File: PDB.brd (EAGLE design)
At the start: 160 x 100 mm, 60 parts, among them IC1 LM555N

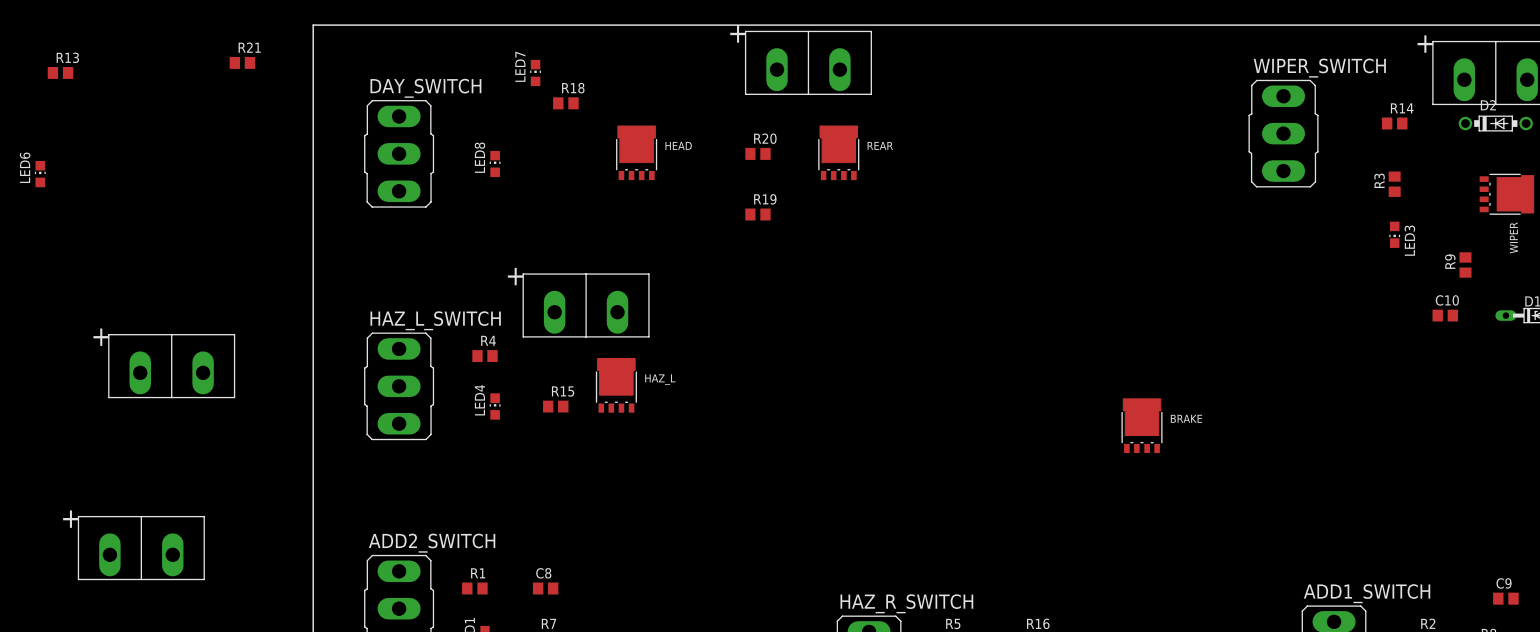
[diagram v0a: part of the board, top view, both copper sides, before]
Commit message: ratsnest to remove some airwires
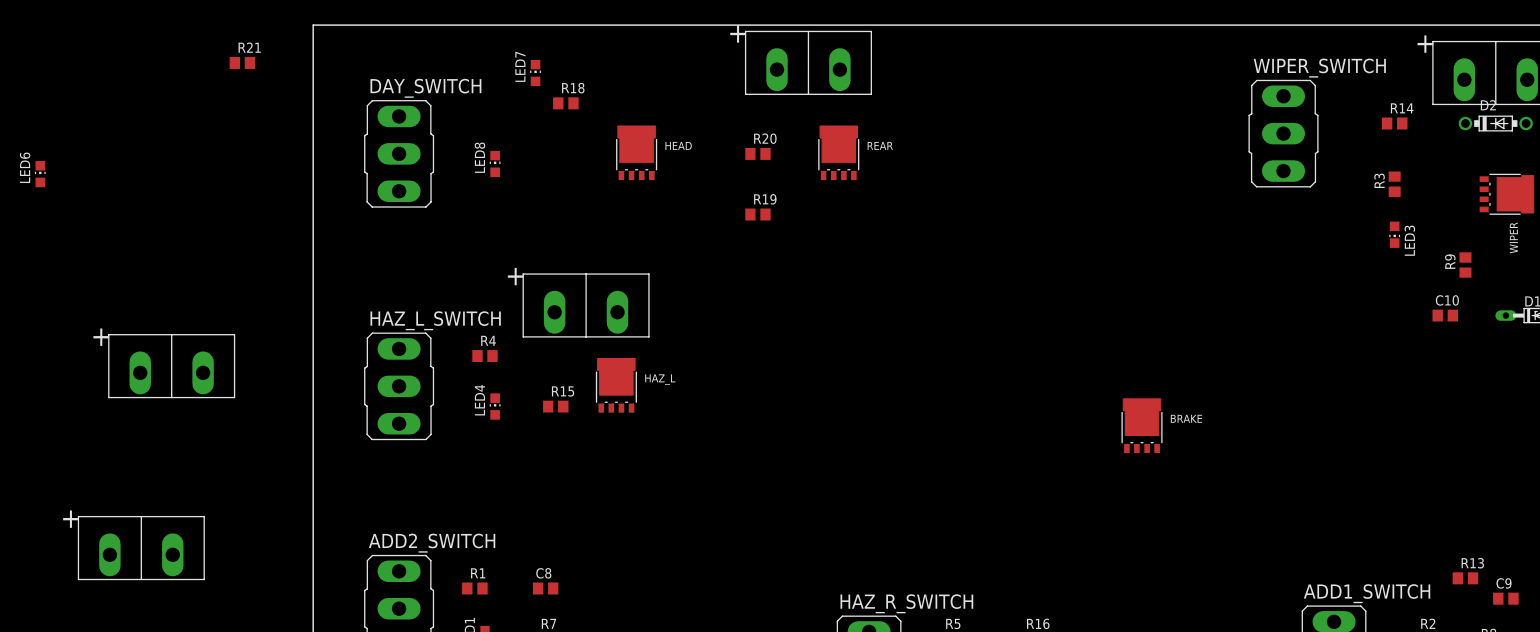
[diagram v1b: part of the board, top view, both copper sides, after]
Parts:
- moved R13 187.6 mm to (144.8, 30.5)

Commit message: updated board layout
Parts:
- removed ADD2_OUT1, ADD2_OUT2, ADD2_OUT3, ADD2_OUT4, ADD2_OUT5, ADD2_OUT6, ADD2_OUT7: POWERPOLE_POWER25A, powerpoles:POWERPOLE_PAIR_25A
- removed BRAKE_SENSOR, DAY_SWITCH: (no value), switch:M9040P
- added ADD1_OUT, BRAKE_OUT, HAZL_OUT, HAZR_OUT, HEADLIGHTS_OUT, REARLIGHTS_OUT, VDD_IN1, WIPER_OUT: POWERPOLE_POWER25A_HORIZONTAL_G2, powerpoles:POWERPOLE_PAIR_25A_HORIZ_G2
- added BRAKE_SNS_OVR, HEADLIGHTS, REARLIGHTS: (no value), switch:M9040P
- ADD2_OUT, VDD_IN: value POWERPOLE_POWER25A -> POWERPOLE_POWER25A_HORIZONTAL_G2; device powerpoles:POWERPOLE_PAIR_25A -> powerpoles:POWERPOLE_PAIR_25A_HORIZ_G2
- moved R21 129.9 mm to (120.7, 85.1)
- moved D2 94.8 mm to (97.8, 7.62)
- moved HAZ_R 94.0 mm to (148.6, 88.9), turned to 180 degrees
- moved LED7 92.7 mm to (120.7, 91.4)
- moved LED5 91.6 mm to (143.5, 82.5), turned to 180 degrees
- moved R5 90.9 mm to (139.7, 91.4), turned to 180 degrees
- moved HAZ_R_SWITCH 82.8 mm to (139.7, 63.5), turned to 180 degrees
- moved R16 79.8 mm to (138.4, 86.4), turned to 180 degrees
- moved BRAKE 78.6 mm to (36.8, 90.2), turned to 270 degrees
- moved R17 78.5 mm to (33.0, 81.3), turned to 270 degrees
- moved D1 77.8 mm to (92.7, 15.2), turned to 180 degrees
- moved VDD_IN 73.7 mm to (-11.4, -3.81), turned to 180 degrees
- moved WIPER 73.4 mm to (105.4, 20.3)
- moved R6 72.6 mm to (25.4, 83.8), turned to 180 degrees
- moved LED8 71.2 mm to (94.0, 85.1)
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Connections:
- new net H8: HEADLIGHTS.1, R18.1
- net GND: now also VDD_IN1.BLACK
- net H1: now also BRAKE_SNS_OVR.1, VDD_IN1.RED; no longer BRAKE_SENSOR.1
- net H7: now also REARLIGHTS.1; no longer DAY_SWITCH.1, R18.1
- net N$1: now also HEADLIGHTS_OUT.BLACK; no longer ADD2_OUT6.BLACK
- net N$17: now also ADD1_OUT.BLACK; no longer ADD2_OUT1.BLACK
- net N$18: now also ADD1_OUT.RED; no longer ADD2_OUT1.RED
- net N$19: now also WIPER_OUT.BLACK; no longer ADD2_OUT2.BLACK
- net N$20: now also WIPER_OUT.RED; no longer ADD2_OUT2.RED
- net N$21: now also HAZL_OUT.BLACK; no longer ADD2_OUT3.BLACK
- net N$23: now also HAZR_OUT.BLACK; no longer ADD2_OUT4.BLACK
- net N$25: now also BRAKE_OUT.BLACK; no longer ADD2_OUT5.BLACK
- net N$3: now also REARLIGHTS_OUT.BLACK; no longer ADD2_OUT7.BLACK
- net VDD: now also BRAKE_OUT.RED, BRAKE_SNS_OVR.2, HAZL_OUT.RED, HAZR_OUT.RED, HEADLIGHTS.2, HEADLIGHTS_OUT.RED, REARLIGHTS.2, REARLIGHTS_OUT.RED; no longer ADD2_OUT3.RED, ADD2_OUT4.RED, ADD2_OUT5.RED, ADD2_OUT6.RED, ADD2_OUT7.RED, BRAKE_SENSOR.2, DAY_SWITCH.2
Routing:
- added copper zone on layer 16, net GND
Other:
- board size 160 x 100 mm -> 209.5 x 127.9 mm

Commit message: board layout
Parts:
- moved ADD2 58.5 mm to (96.5, 25.4), turned to 270 degrees
- moved R1 49.7 mm to (87.6, 15.2)
- moved LED1 48.1 mm to (86.4, 22.9), turned to 180 degrees
- moved ADD2_OUT 40.8 mm to (83.8, -1.27)
- moved ADD2_SWITCH 39.4 mm to (88.3, 41.9)
- moved VDD_IN 38.1 mm to (26.7, -2.54)
- moved C8 32.0 mm to (78.7, 22.9)
- moved R7 32.0 mm to (78.7, 16.5)
- moved R12 30.6 mm to (81.3, 29.2)
- moved D1 22.9 mm to (111.8, 27.9)
- moved WIPER_OUT 19.7 mm to (116.8, -1.27)
- moved C10 19.4 mm to (114.3, 22.9)
- moved D2 19.4 mm to (116.8, 11.4)
- moved ADD1 19.1 mm to (149.9, 27.9), turned to 270 degrees
- moved R3 19.1 mm to (128.3, 27.9)
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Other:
- board size 209.5 x 127.9 mm -> 198.1 x 127.9 mm

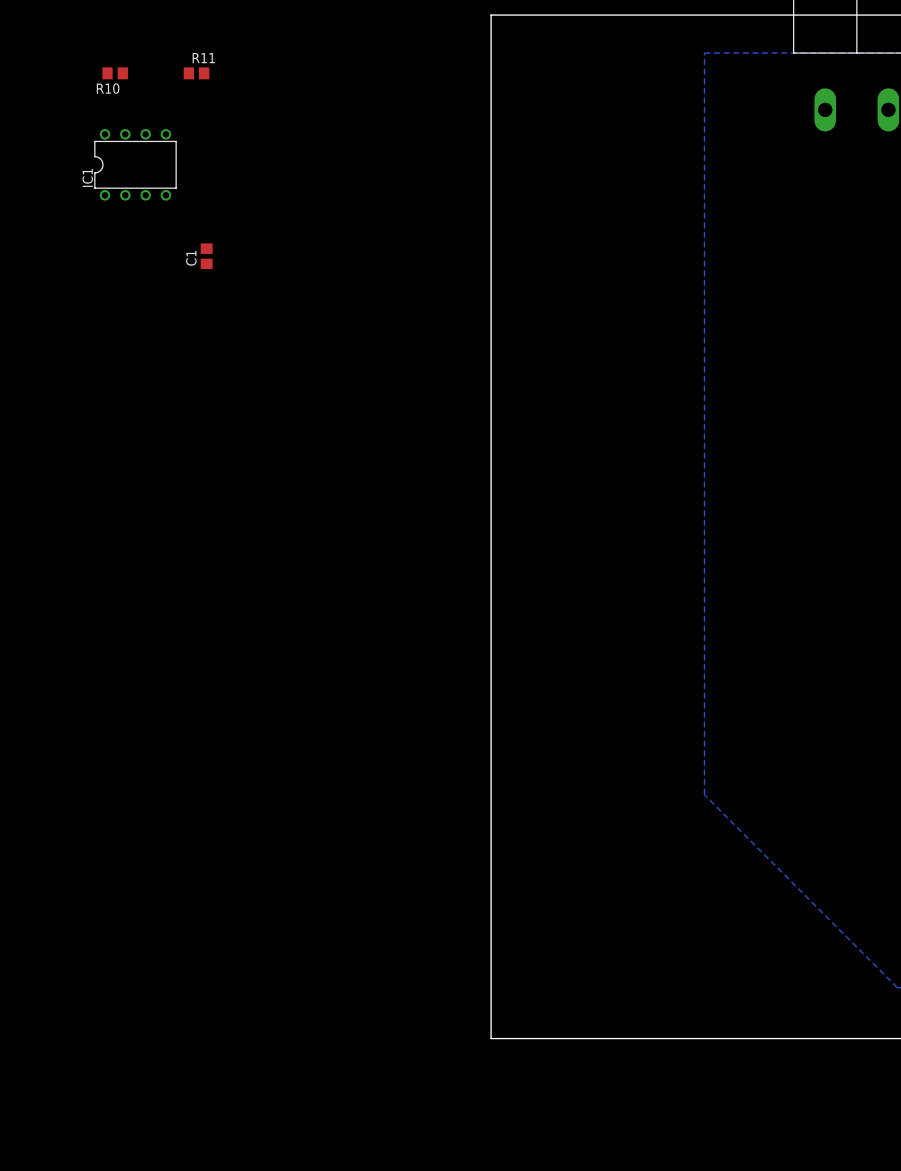
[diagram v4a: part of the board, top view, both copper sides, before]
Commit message: added trim pot
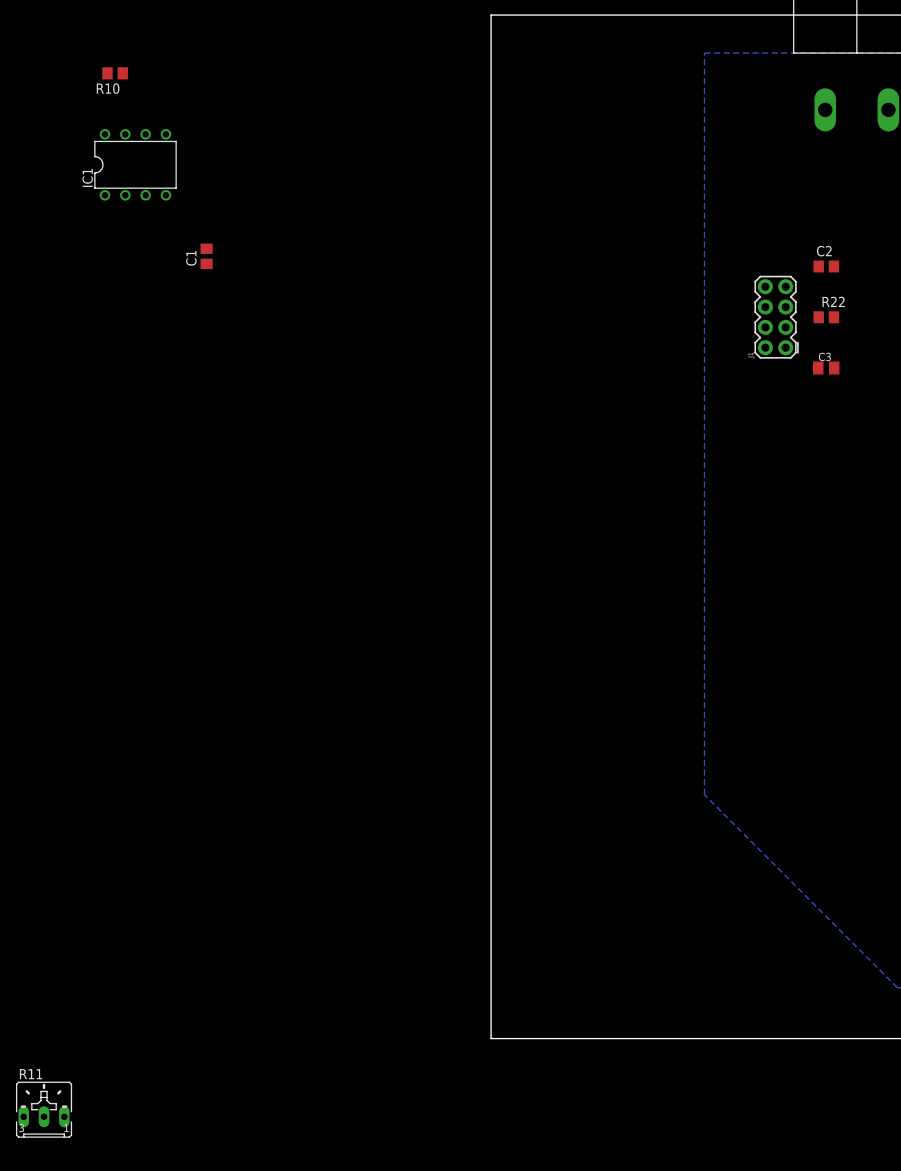
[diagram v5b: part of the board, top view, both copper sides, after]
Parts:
- added C2: 0.01uF, rcl:C0805
- added C3: 10uF, rcl:C0805K
- added J1: (no value), SparkFun-Connectors:2X4
- added R22: 1K, rcl:R0805
- R11: device rcl:R0805 -> pot:B25U
- moved R11 130.9 mm to (-94.0, -21.6)
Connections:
- removed net N$4: C1.1, IC1.2, IC1.6, R11.2
- removed net N$5: IC1.7, R10.1, R11.1
- removed net N$6: IC1.8, R10.2
- new net CV: C2.1, IC1.5, J1.8
- new net DIS: IC1.7, J1.4, R10.1, R11.A
- new net Q: IC1.3, J1.5, R22.1
- new net R: IC1.4, IC1.8, J1.7, R10.2
- new net TR/THR: C1.1, C3.1, IC1.2, IC1.6, J1.3, J1.6, R11.S
- new net V+: J1.2
- net 555_OUT: now also R22.2; no longer IC1.3
- net GND: now also C2.2, C3.2, J1.1, R11.E

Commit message: changed PDB
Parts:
- removed IC1: LM555N, linear:DIL08
- removed J1: (no value), SparkFun-Connectors:2X4
- added J2, J3: (no value), SparkFun-Connectors:1X04_LONGPADS
- moved R10 151.8 mm to (53.3, 45.7), turned to 90 degrees
- moved R11 146.2 mm to (44.5, 25.4), turned to 180 degrees
- moved C1 118.2 mm to (36.8, 43.2), turned to 180 degrees
- moved R22 64.9 mm to (53.3, 35.6)
- moved C3 58.2 mm to (53.3, 40.6)
- moved C2 56.4 mm to (36.8, 38.1), turned to 180 degrees
- moved VDD_IN1 47.4 mm to (14.0, 63.5), turned to 90 degrees
- moved R18 27.1 mm to (111.8, 83.8)
- moved VDD_IN 22.9 mm to (49.5, -1.27)
- moved R4 19.2 mm to (69.8, 77.5), turned to 270 degrees
- moved R6 17.3 mm to (38.1, 77.5), turned to 270 degrees
- moved LED4 16.6 mm to (63.5, 77.5), turned to 0 degrees
- moved R5 16.5 mm to (146.1, 76.2), turned to 270 degrees
- moved R1 15.5 mm to (96.5, 27.9), turned to 90 degrees
- moved R20 15.3 mm to (92.7, 76.2), turned to 90 degrees
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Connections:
- removed net R: IC1.4, IC1.8, J1.7, R10.2
- net CV: now also J3.3; no longer IC1.5, J1.8
- net DIS: now also J2.3; no longer IC1.7, J1.4
- net GND: now also J3.4; no longer IC1.1, J1.1
- net Q: now also J2.4; no longer IC1.3, J1.5
- net TR/THR: now also J2.2, J3.1; no longer IC1.2, IC1.6, J1.3, J1.6
- net V+: now also J2.1, J3.2, R10.2; no longer J1.2
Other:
- board size 198.1 x 127.9 mm -> 146 x 125.4 mm

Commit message: modified ground plane in PDB
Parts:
- removed R15, R16: 220, rcl:R0805
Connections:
- removed net N$12: HAZ_R.4, LED5.A, R16.2
- removed net N$24: HAZ_L.4, LED4.A, R15.2
- net H2: now also HAZ_R.4, LED5.A; no longer R16.1
- net H3: now also HAZ_L.4, LED4.A; no longer R15.1
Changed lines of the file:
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@@
 <attribute name="SPICEPREFIX" value="R" x="121.92" y="27.94" size="1.778" layer="27" display="off"/>
-</element>
-<element name="R15" library="rcl" library_urn="urn:adsk.eagle:library:334" package="R0805" package3d_urn="urn:adsk.eagle:package:23553/2" value="220" x="57.15" y="82.55">
-<attribute name="SPICEPREFIX" value="R" x="57.15" y="82.55" size="1.778" layer="27" display="off"/>
-</element>
-<element name="R16" library="rcl" library_urn="urn:adsk.eagle:library:334" package="R0805" package3d_urn="urn:adsk.eagle:package:23553/2" value="220" x="138.43" y="82.55">
-<attribute name="SPICEPREFIX" value="R" x="138.43" y="82.55" size="1.778" layer="27" display="off"/>
 </element>
 <element name="R17" library="rcl" library_urn="urn:adsk.eagle:library:334" package="R0805" package3d_urn="urn:adsk.eagle:package:23553/2" value="" x="25.4" y="82.55">
@@
 <contactref element="R20" pad="1"/>
 <contactref element="VDD_IN1" pad="BLACK"/>
-<polygon width="0.1524" layer="16">
-<vertex x="17.78" y="12.7"/>
-<vertex x="17.78" y="110.49"/>
-<vertex x="153.67" y="110.49"/>
-<vertex x="153.67" y="-6.35"/>
-<vertex x="36.83" y="-6.35"/>
-</polygon>
 <contactref element="R11" pad="E"/>
 <contactref element="J3" pad="4"/>
 <contactref element="C2" pad="2"/>
 <contactref element="C3" pad="2"/>
+<polygon width="0.1524" layer="16">
+<vertex x="68.58" y="1.27"/>
+<vertex x="33.02" y="1.27" curve="-90"/>
+<vertex x="16.51" y="17.78"/>
+<vertex x="16.51" y="101.6" curve="-90"/>
+<vertex x="24.13" y="109.22"/>
+<vertex x="142.24" y="109.22" curve="-90"/>
+<vertex x="152.4" y="99.06"/>
+<vertex x="152.4" y="5.08" curve="-90"/>
+<vertex x="148.59" y="1.27"/>
+</polygon>
 <wire x1="138.245" y1="90.806" x2="138.245" y2="92.075" width="0" layer="19" extent="1-1"/>
 <wire x1="138.245" y1="89.535" x2="138.245" y2="90.806" width="0" layer="19" extent="1-1"/>
@@
 <wire x1="25.215" y1="97.155" x2="25.215" y2="95.886" width="0" layer="19" extent="1-1"/>
 <wire x1="21.07" y1="59.55" x2="38.1" y2="76.52" width="0" layer="19" extent="1-1"/>
-<wire x1="35.88" y1="43.18" x2="21.07" y2="59.55" width="0" layer="19" extent="1-1"/>
-<wire x1="35.88" y1="38.1" x2="35.88" y2="43.18" width="0" layer="19" extent="1-1"/>
-<wire x1="41.91" y1="35.56" x2="35.88" y2="38.1" width="0" layer="19" extent="1-1"/>
-<wire x1="46.99" y1="26.289" x2="41.91" y2="35.56" width="0" layer="19" extent="1-1"/>
-<wire x1="54.34" y1="40.64" x2="41.91" y2="35.56" width="0" layer="19" extent="1-1"/>
-<wire x1="53.48" y1="5.83" x2="46.99" y2="26.289" width="0" layer="19" extent="1-1"/>
-<wire x1="79.69" y1="21.59" x2="53.48" y2="5.83" width="0" layer="19" extent="1-1"/>
-<wire x1="88.715" y1="20.955" x2="79.69" y2="21.59" width="0" layer="19" extent="1-1"/>
-<wire x1="88.715" y1="19.686" x2="88.715" y2="20.955" width="0" layer="19" extent="1-1"/>
-<wire x1="88.715" y1="18.415" x2="88.715" y2="19.686" width="0" layer="19" extent="1-1"/>
-<wire x1="96.52" y1="28.89" x2="88.715" y2="20.955" width="0" layer="19" extent="1-1"/>
-<wire x1="107.95" y1="27.94" x2="96.52" y2="28.89" width="0" layer="19" extent="1-1"/>
+<wire x1="35.88" y1="38.1" x2="41.91" y2="35.56" width="0" layer="19" extent="1-1"/>
+<wire x1="35.88" y1="43.18" x2="35.88" y2="38.1" width="0" layer="19" extent="1-1"/>
 <wire x1="113.35" y1="22.86" x2="107.95" y2="27.94" width="0" layer="19" extent="1-1"/>
 <wire x1="121.735" y1="20.955" x2="113.35" y2="22.86" width="0" layer="19" extent="1-1"/>
@@
 <wire x1="121.735" y1="18.415" x2="121.735" y2="19.686" width="0" layer="19" extent="1-1"/>
 <wire x1="128.27" y1="26.99" x2="121.735" y2="20.955" width="0" layer="19" extent="1-1"/>
+<wire x1="96.52" y1="28.89" x2="107.95" y2="27.94" width="0" layer="19" extent="1-1"/>
+<wire x1="88.715" y1="20.955" x2="96.52" y2="28.89" width="0" layer="19" extent="1-1"/>
+<wire x1="88.715" y1="19.686" x2="88.715" y2="20.955" width="0" layer="19" extent="1-1"/>
+<wire x1="88.715" y1="18.415" x2="88.715" y2="19.686" width="0" layer="19" extent="1-1"/>
+<wire x1="79.69" y1="21.59" x2="88.715" y2="20.955" width="0" layer="19" extent="1-1"/>
 <wire x1="136.84" y1="17.78" x2="128.27" y2="26.99" width="0" layer="19" extent="1-1"/>
 <wire x1="143.325" y1="18.415" x2="136.84" y2="17.78" width="0" layer="19" extent="1-1"/>
@@
 <wire x1="143.325" y1="20.955" x2="143.325" y2="19.686" width="0" layer="19" extent="1-1"/>
 <wire x1="143.51" y1="28.26" x2="143.325" y2="20.955" width="0" layer="19" extent="1-1"/>
+<wire x1="54.34" y1="40.64" x2="41.91" y2="35.56" width="0" layer="19" extent="1-1"/>
 </signal>
 <signal name="VDD">
@@
 <signal name="H3">
 <contactref element="HAZ_L_SWITCH" pad="1"/>
-<contactref element="R15" pad="1"/>
-<wire x1="62.865" y1="68.199" x2="56.2" y2="82.55" width="0" layer="19" extent="1-1"/>
+<contactref element="HAZ_L" pad="4"/>
+<contactref element="LED4" pad="A"/>
+<wire x1="63.5" y1="76.42" x2="56.965" y2="90.805" width="0" layer="19" extent="1-1"/>
+<wire x1="62.865" y1="68.199" x2="63.5" y2="76.42" width="0" layer="19" extent="1-1"/>
 </signal>
 <signal name="H5">
@@
 <signal name="H2">
 <contactref element="HAZ_R_SWITCH" pad="1"/>
-<contactref element="R16" pad="1"/>
-<wire x1="139.7" y1="58.801" x2="137.48" y2="82.55" width="0" layer="19" extent="1-1"/>
+<contactref element="HAZ_R" pad="4"/>
+<contactref element="LED5" pad="A"/>
+<wire x1="140.97" y1="75.15" x2="138.245" y2="88.265" width="0" layer="19" extent="1-1"/>
+<wire x1="139.7" y1="58.801" x2="140.97" y2="75.15" width="0" layer="19" extent="1-1"/>
 </signal>
 <signal name="H4">
@@
 <wire x1="140.97" y1="77.25" x2="146.05" y2="77.15" width="0" layer="19" extent="1-1"/>
 </signal>
-<signal name="N$12">
-<contactref element="HAZ_R" pad="4"/>
-<contactref element="R16" pad="2"/>
-<contactref element="LED5" pad="A"/>
-<wire x1="139.38" y1="82.55" x2="138.245" y2="88.265" width="0" layer="19" extent="1-1"/>
-<wire x1="140.97" y1="75.15" x2="139.38" y2="82.55" width="0" layer="19" extent="1-1"/>
-</signal>
 <signal name="N$13">
 <contactref element="BRAKE" pad="4"/>
@@
 <wire x1="121.735" y1="17.145" x2="122.87" y2="27.94" width="0" layer="19" extent="1-1"/>
 </signal>
-<signal name="N$24">
-<contactref element="HAZ_L" pad="4"/>
-<contactref element="R15" pad="2"/>
-<contactref element="LED4" pad="A"/>
-<wire x1="58.1" y1="82.55" x2="56.965" y2="90.805" width="0" layer="19" extent="1-1"/>
-<wire x1="63.5" y1="76.42" x2="58.1" y2="82.55" width="0" layer="19" extent="1-1"/>
-</signal>
 <signal name="N$26">
